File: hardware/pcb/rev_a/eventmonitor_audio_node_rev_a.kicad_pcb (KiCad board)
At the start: 4 copper layers, 65 x 50 mm, 37 parts, among them J1 USB-C USB2.0, Q1 BC847B, Q2 BC847B, SW1 BOOT, SW2 RESET, U1 ESP32-S3-WROOM-1U-N16R8, U2 CP2102N-A02-GQFN24R, U3 AMS1117-3.3, U4 USBLC6-2SC6, U5 ICS-43434

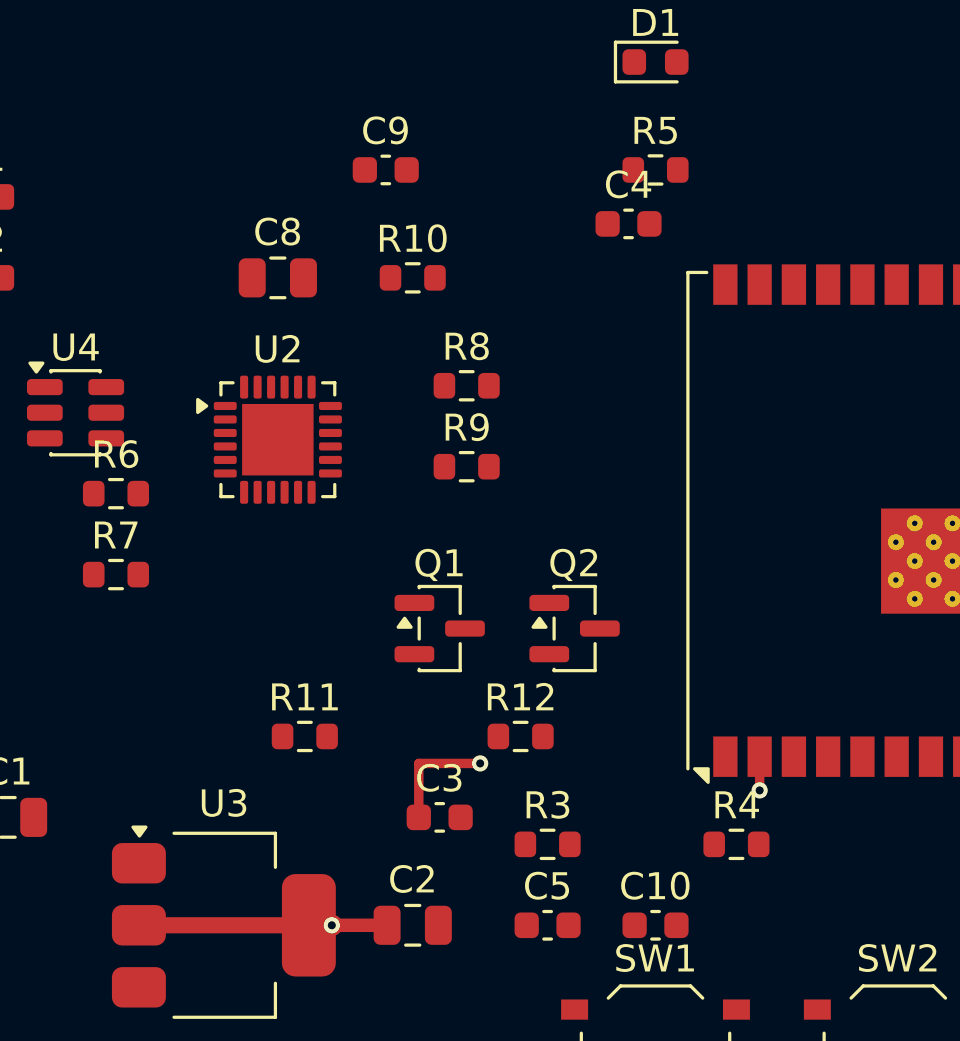
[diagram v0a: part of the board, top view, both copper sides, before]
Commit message: feat(pcb): extend Rev-A 3V3 plane routing
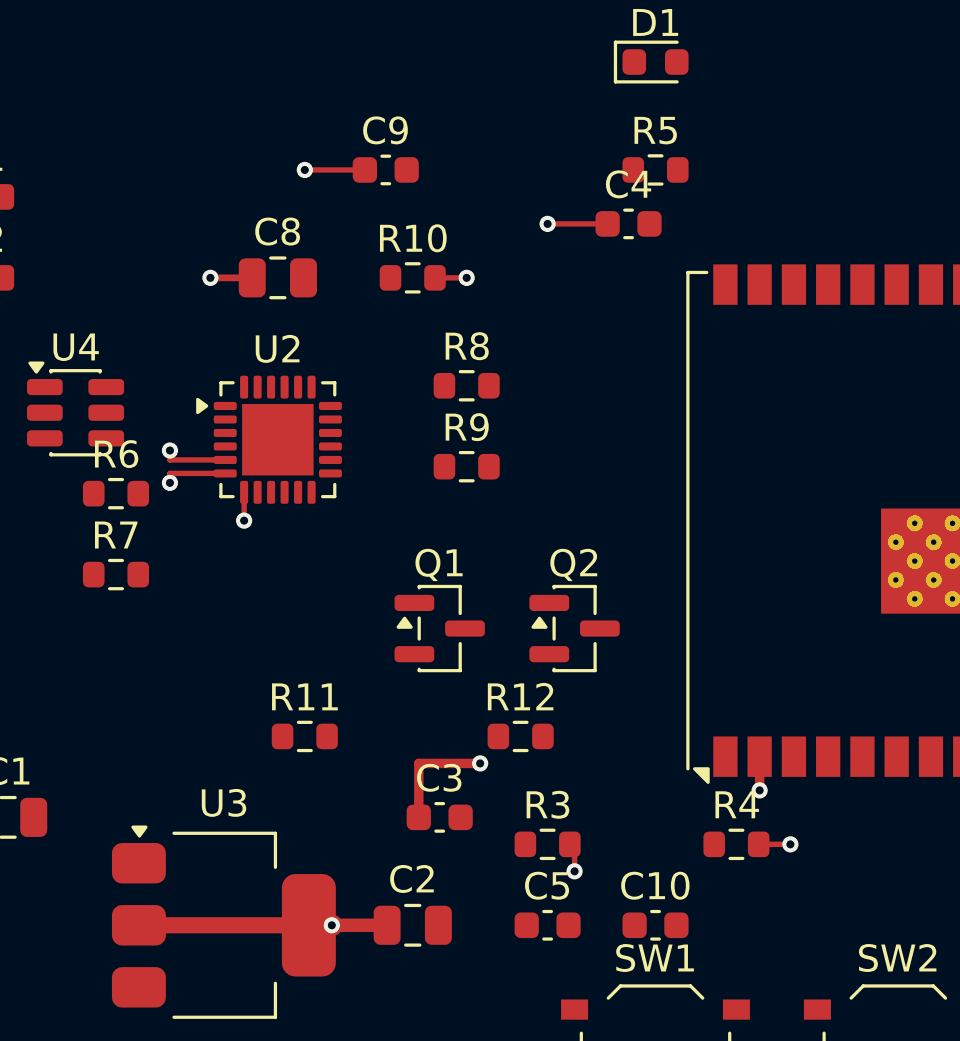
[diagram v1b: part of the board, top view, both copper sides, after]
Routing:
- net +3V3: track 27.4 -> 42.7 mm, vias 4 -> 13

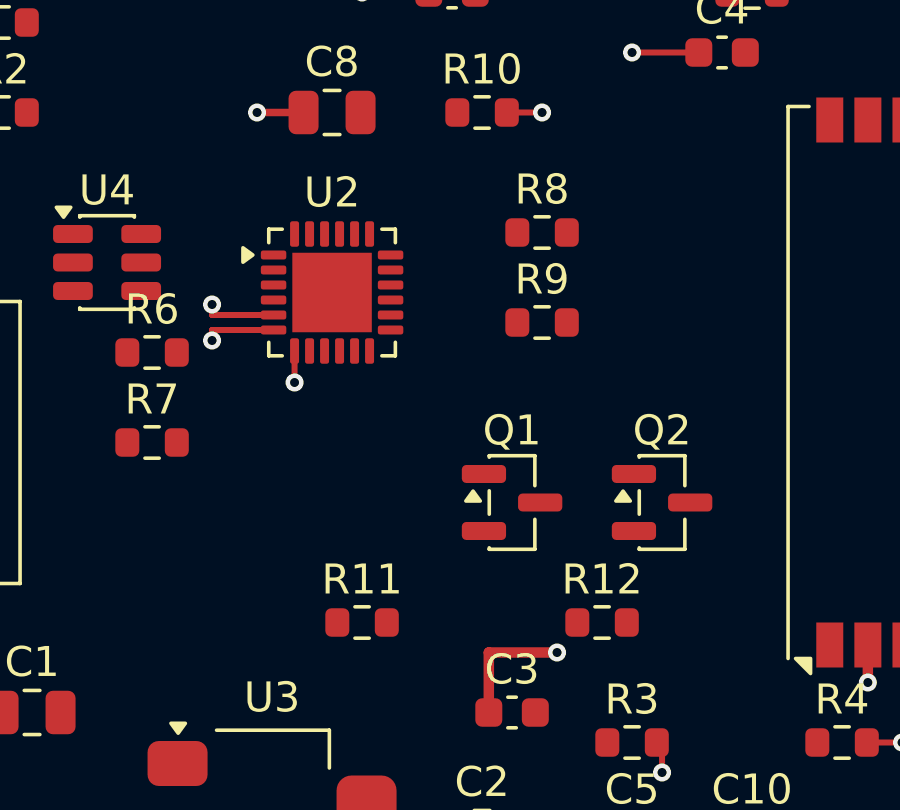
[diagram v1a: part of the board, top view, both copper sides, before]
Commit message: feat(pcb): route CP2102N auto-program controls
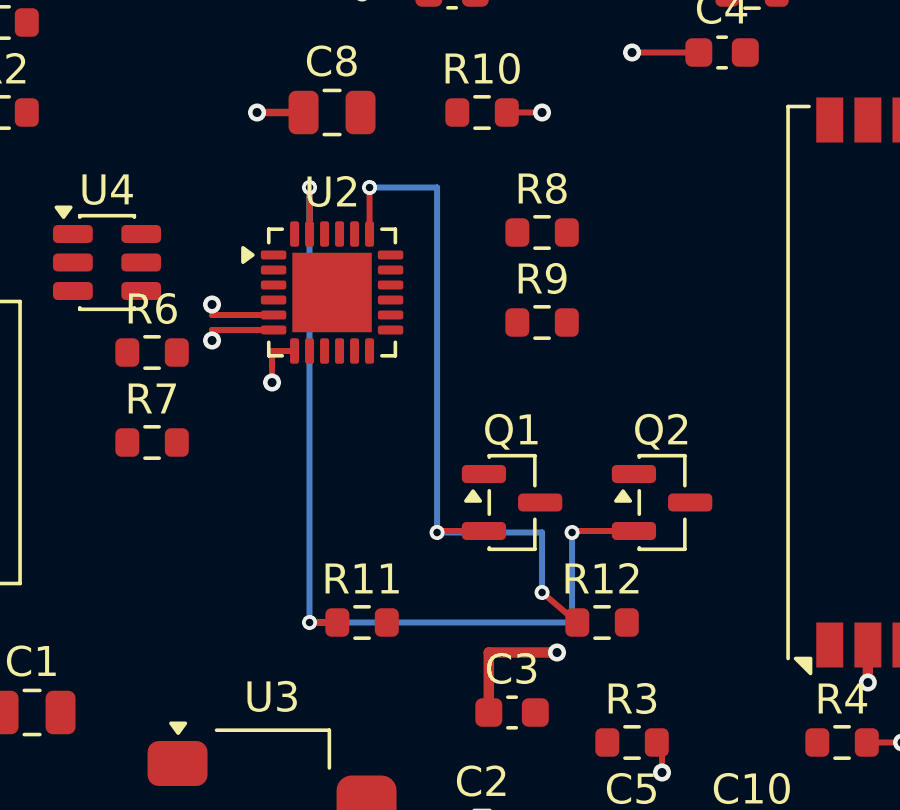
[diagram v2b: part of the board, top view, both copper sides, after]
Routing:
- net AUTO_DTR: track 0.00 -> 30.8 mm, vias 0 -> 3
- net AUTO_RTS: track 0.00 -> 24.0 mm, vias 0 -> 3
- net +3V3: track 42.7 -> 43.5 mm

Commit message: feat(pcb): route Rev-A status LED
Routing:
- net LED_A: track 0.00 -> 5.61 mm

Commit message: feat(pcb): route Rev-A auto-program transistor bases
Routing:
- net Q2_BASE: track 0.00 -> 16.3 mm
- net Q1_BASE: track 0.00 -> 10.1 mm

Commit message: feat(pcb): route Rev-A manual boot control
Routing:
- net BOOT: track 0.00 -> 13.0 mm

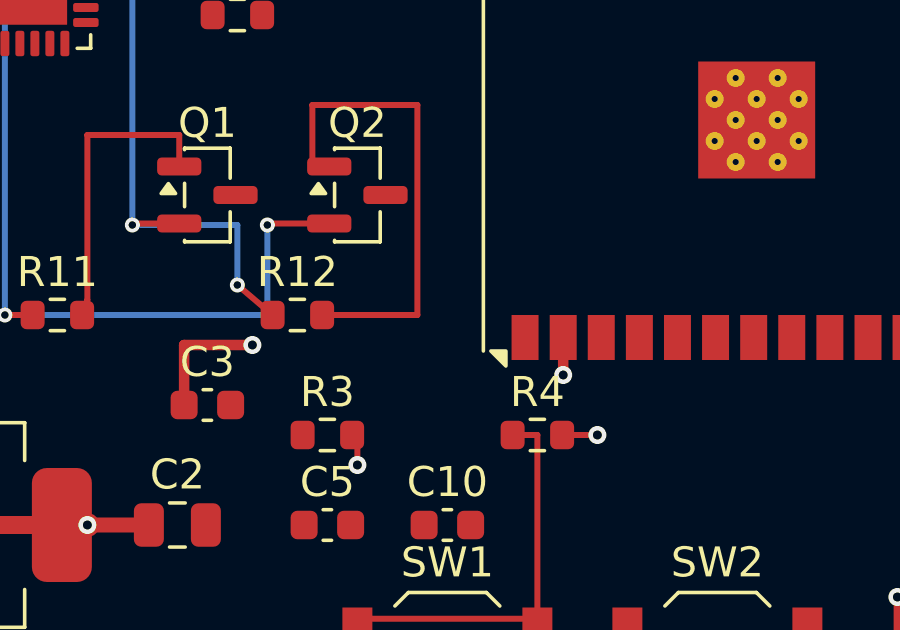
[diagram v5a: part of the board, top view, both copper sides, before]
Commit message: feat(pcb): route Rev-A boot transistor path
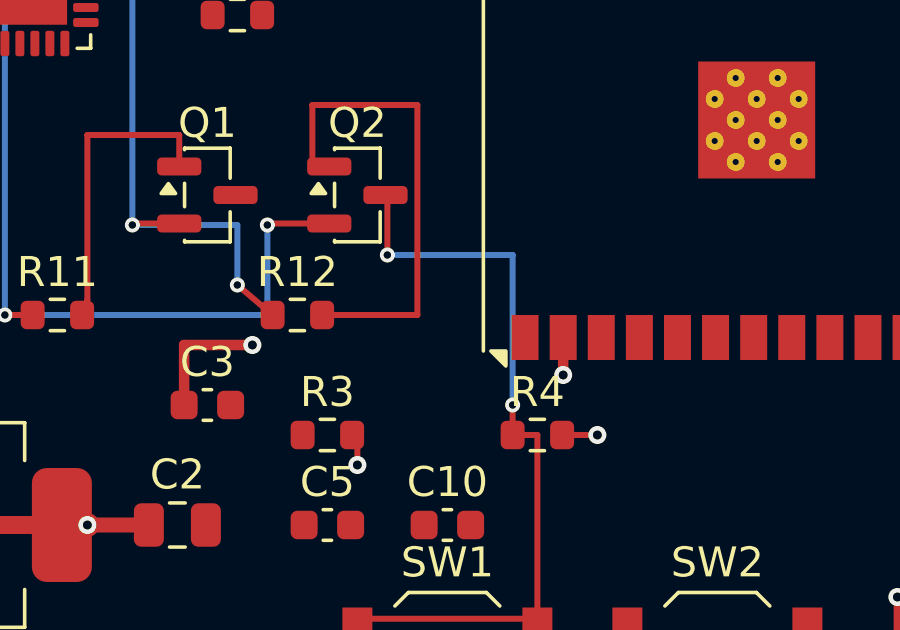
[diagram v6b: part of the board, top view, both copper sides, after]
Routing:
- net BOOT: track 13.0 -> 25.2 mm, vias 0 -> 2

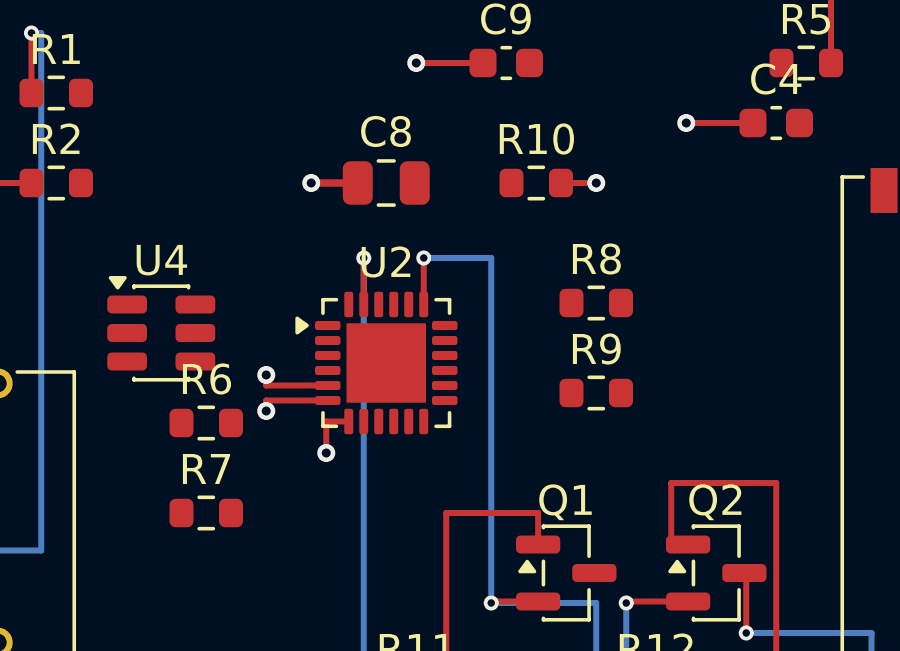
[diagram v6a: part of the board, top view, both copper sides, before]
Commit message: feat(pcb): route Rev-A CP2102N reset
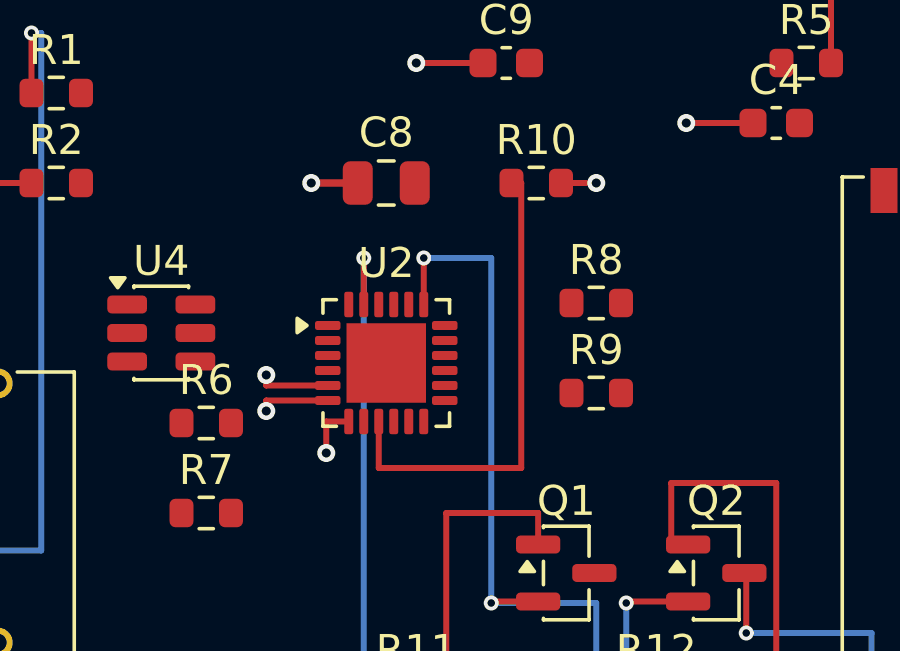
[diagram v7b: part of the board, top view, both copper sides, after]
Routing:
- net U2_RST: track 0.00 -> 16.1 mm

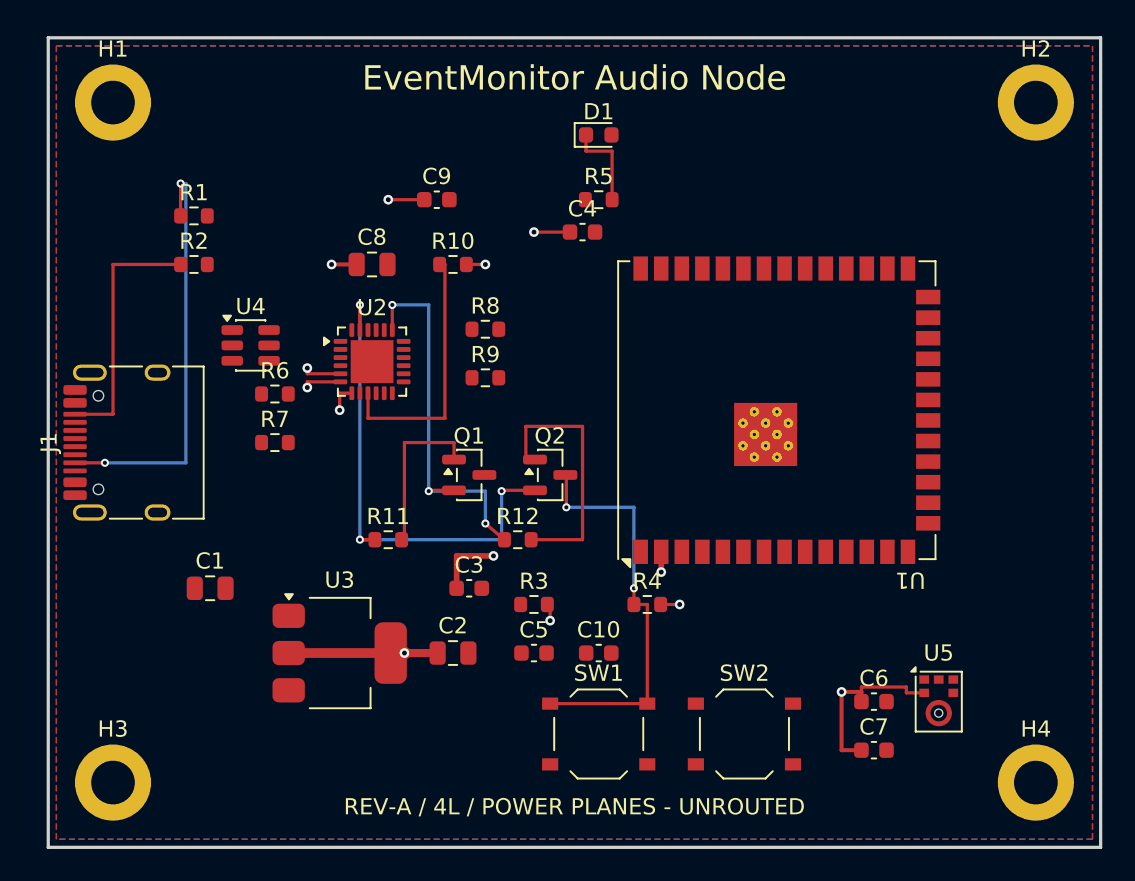
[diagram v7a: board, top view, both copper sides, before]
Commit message: feat(pcb): route Rev-A ESP32 peripheral signals
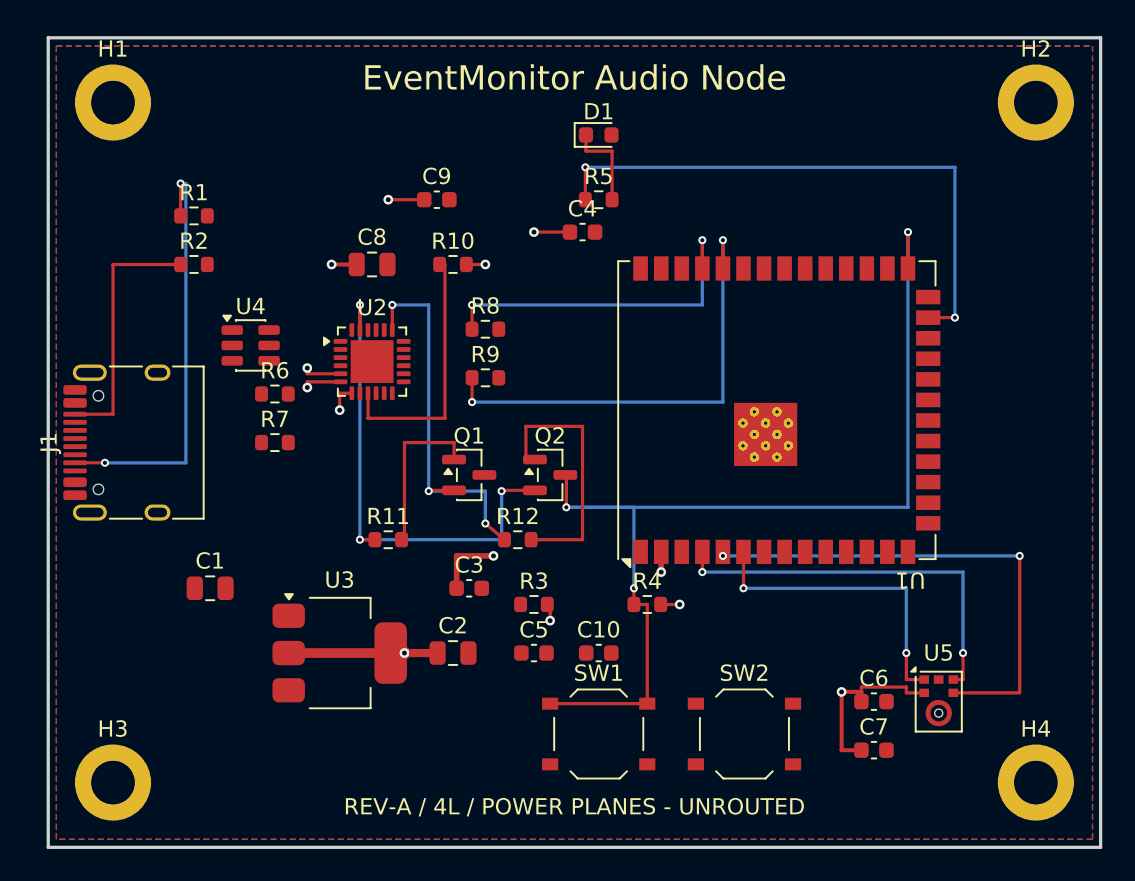
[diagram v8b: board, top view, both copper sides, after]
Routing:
- net BOOT: track 25.2 -> 65.5 mm, vias 2 -> 3
- net LED_STATUS: track 0.00 -> 35.8 mm, vias 0 -> 2
- net I2S_BCLK: track 0.00 -> 31.1 mm, vias 0 -> 2
- net UART_RX_ESP: track 0.00 -> 28.7 mm, vias 0 -> 2
- net I2S_WS: track 0.00 -> 24.6 mm, vias 0 -> 2
- net UART_TX_ESP: track 0.00 -> 21.5 mm, vias 0 -> 2
- net I2S_DATA: track 0.00 -> 19.0 mm, vias 0 -> 2
